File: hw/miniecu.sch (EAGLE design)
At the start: 60 parts

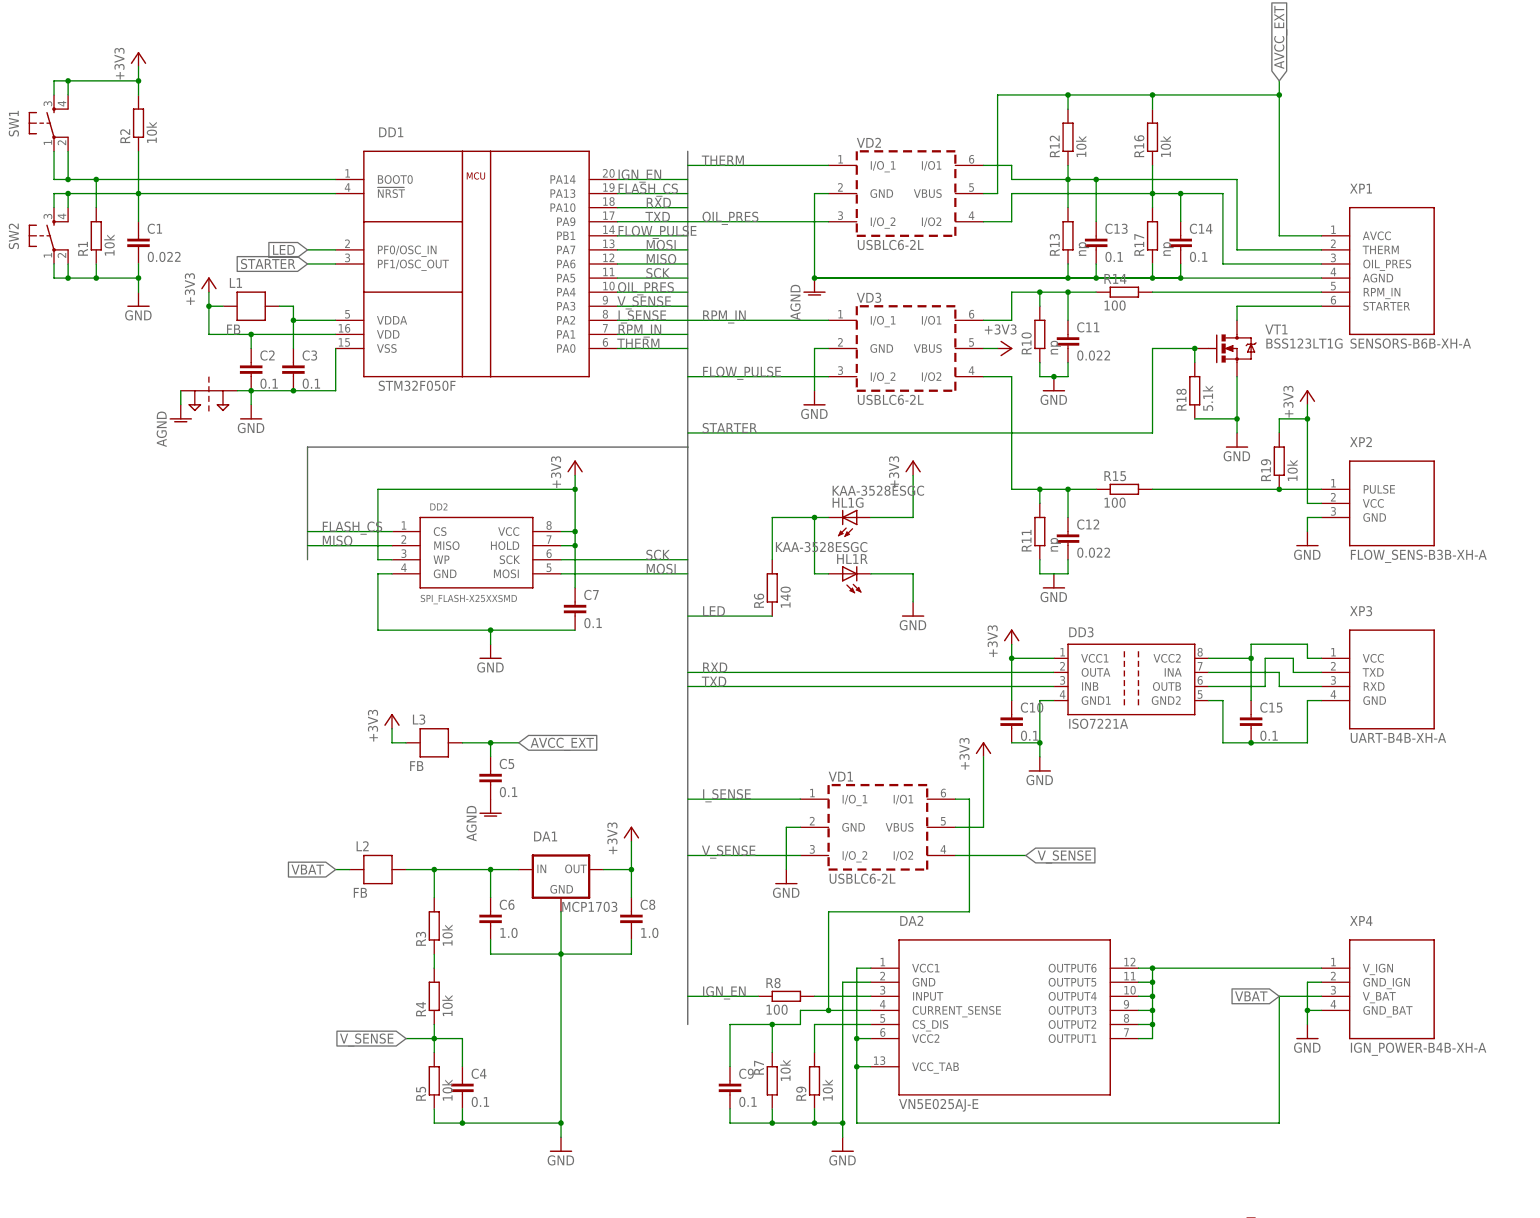
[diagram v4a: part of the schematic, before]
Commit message: sch: minimize BOM (by resistor values)
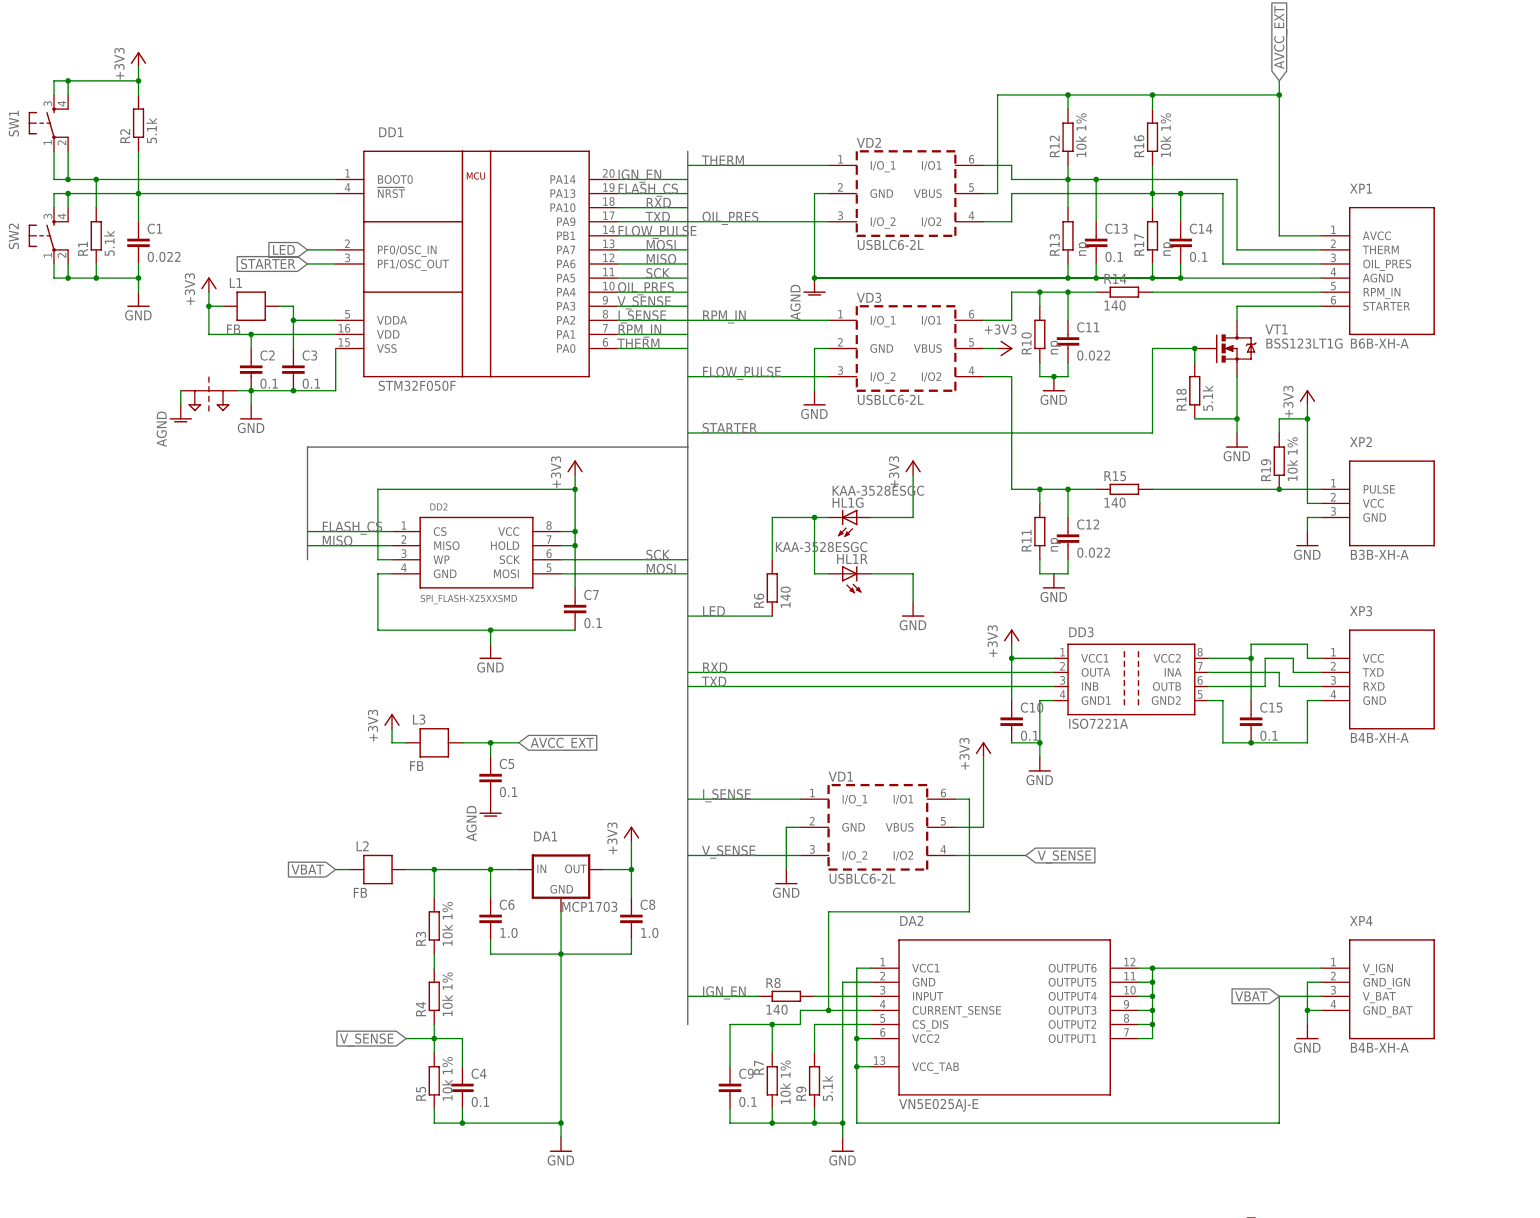
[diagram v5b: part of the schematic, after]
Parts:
- C1: device resistor:C-EUC0805 -> resistor:C-EUC0603
- R1, R2, R9: value 10k -> 5.1k
- R12, R16, R19, R3, R4, R5, R7: value 10k -> 10k 1%
- R14, R15, R8: value 100 -> 140
- XP1: value SENSORS-B6B-XH-A -> B6B-XH-A
- XP2: value FLOW_SENS-B3B-XH-A -> B3B-XH-A
- XP3: value UART-B4B-XH-A -> B4B-XH-A
- XP4: value IGN_POWER-B4B-XH-A -> B4B-XH-A
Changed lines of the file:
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@@
 <part name="DD2" library="SparkFun-DigitalIC" deviceset="SPI_FLASH-X25XX" device="SMD"/>
 <part name="DD3" library="texas" deviceset="ISO7221" device="" technology="A"/>
-<part name="XP2" library="miniecu-con" deviceset="FLOW_SENS" device="-B3B-XH-A"/>
-<part name="XP4" library="miniecu-con" deviceset="IGN_POWER" device="-B4B-XH-A"/>
-<part name="XP1" library="miniecu-con" deviceset="SENSORS" device="-B6B-XH-A"/>
-<part name="XP3" library="miniecu-con" deviceset="UART" device="-B4B-XH-A"/>
+<part name="XP2" library="miniecu-con" deviceset="FLOW_SENS" device="-B3B-XH-A" value="B3B-XH-A"/>
+<part name="XP4" library="miniecu-con" deviceset="IGN_POWER" device="-B4B-XH-A" value="B4B-XH-A"/>
+<part name="XP1" library="miniecu-con" deviceset="SENSORS" device="-B6B-XH-A" value="B6B-XH-A"/>
+<part name="XP3" library="miniecu-con" deviceset="UART" device="-B4B-XH-A" value="B4B-XH-A"/>
 <part name="C15" library="resistor" deviceset="C-EU" device="C0603" value="0.1"/>
 <part name="C10" library="resistor" deviceset="C-EU" device="C0603" value="0.1"/>
@@
 <part name="GND6" library="supply1" deviceset="GND" device=""/>
 <part name="R18" library="resistor" deviceset="R-EU_" device="R0603" value="5.1k"/>
-<part name="R14" library="resistor" deviceset="R-EU_" device="R0603" value="100"/>
+<part name="R14" library="resistor" deviceset="R-EU_" device="R0603" value="140"/>
 <part name="R10" library="resistor" deviceset="R-EU_" device="R0603" value="np"/>
 <part name="C11" library="resistor" deviceset="C-EU" device="C0603" value="0.022"/>
-<part name="R16" library="resistor" deviceset="R-EU_" device="R0805" value="10k"/>
-<part name="R12" library="resistor" deviceset="R-EU_" device="R0805" value="10k"/>
+<part name="R16" library="resistor" deviceset="R-EU_" device="R0805" value="10k 1%"/>
+<part name="R12" library="resistor" deviceset="R-EU_" device="R0805" value="10k 1%"/>
 <part name="R13" library="resistor" deviceset="R-EU_" device="R0805" value="np"/>
 <part name="R17" library="resistor" deviceset="R-EU_" device="R0805" value="np"/>
@@
 <part name="C13" library="resistor" deviceset="C-EU" device="C0603" value="0.1"/>
 <part name="GND7" library="supply1" deviceset="GND" device=""/>
-<part name="R15" library="resistor" deviceset="R-EU_" device="R0603" value="100"/>
+<part name="R15" library="resistor" deviceset="R-EU_" device="R0603" value="140"/>
 <part name="R11" library="resistor" deviceset="R-EU_" device="R0603" value="np"/>
 <part name="C12" library="resistor" deviceset="C-EU" device="C0603" value="0.022"/>
@@
 <part name="C5" library="resistor" deviceset="C-EU" device="C0603" value="0.1"/>
 <part name="+3V7" library="supply1" deviceset="+3V3" device=""/>
-<part name="C1" library="resistor" deviceset="C-EU" device="C0805" value="0.022"/>
+<part name="C1" library="resistor" deviceset="C-EU" device="C0603" value="0.022"/>
 <part name="GND10" library="supply1" deviceset="GND" device=""/>
 <part name="SW1" library="SparkFun-Electromechanical" deviceset="TAC_SWITCH" device="SMD"/>
@@
 <part name="C8" library="resistor" deviceset="C-EU" device="C0805" value="1.0"/>
 <part name="+3V9" library="supply1" deviceset="+3V3" device=""/>
-<part name="R4" library="resistor" deviceset="R-EU_" device="R0805" value="10k"/>
-<part name="R5" library="resistor" deviceset="R-EU_" device="R0805" value="10k"/>
+<part name="R4" library="resistor" deviceset="R-EU_" device="R0805" value="10k 1%"/>
+<part name="R5" library="resistor" deviceset="R-EU_" device="R0805" value="10k 1%"/>
 <part name="C4" library="resistor" deviceset="C-EU" device="C0603" value="0.1"/>
 <part name="VD1" library="usblc6" deviceset="USBLC6-2" device="SC6" value="USBLC6-2L"/>
 <part name="GND12" library="supply1" deviceset="GND" device=""/>
 <part name="DA2" library="power-ic" deviceset="VN5E025AJ" device="-E"/>
-<part name="R8" library="resistor" deviceset="R-EU_" device="R0603" value="100"/>
+<part name="R8" library="resistor" deviceset="R-EU_" device="R0603" value="140"/>
 <part name="GND13" library="supply1" deviceset="GND" device=""/>
-<part name="R9" library="resistor" deviceset="R-EU_" device="R0603" value="10k"/>
-<part name="R7" library="resistor" deviceset="R-EU_" device="R0805" value="10k"/>
+<part name="R9" library="resistor" deviceset="R-EU_" device="R0603" value="5.1k"/>
+<part name="R7" library="resistor" deviceset="R-EU_" device="R0805" value="10k 1%"/>
 <part name="C9" library="resistor" deviceset="C-EU" device="C0603" value="0.1"/>
 <part name="FRAME1" library="SparkFun-Aesthetics" deviceset="FRAME-A3" device=""/>
-<part name="R19" library="resistor" deviceset="R-EU_" device="R0805" value="10k"/>
+<part name="R19" library="resistor" deviceset="R-EU_" device="R0805" value="10k 1%"/>
 <part name="HL1" library="led2" deviceset="KAA-3528ESGC" device=""/>
 <part name="GND14" library="supply1" deviceset="GND" device=""/>
@@
 <part name="H3" library="holes" deviceset="MOUNT-HOLE" device="3.2"/>
 <part name="H4" library="holes" deviceset="MOUNT-HOLE" device="3.2"/>
-<part name="R1" library="resistor" deviceset="R-EU_" device="R0603" value="10k"/>
-<part name="R2" library="resistor" deviceset="R-EU_" device="R0603" value="10k"/>
+<part name="R1" library="resistor" deviceset="R-EU_" device="R0603" value="5.1k"/>
+<part name="R2" library="resistor" deviceset="R-EU_" device="R0603" value="5.1k"/>
 <part name="+3V10" library="supply1" deviceset="+3V3" device=""/>
-<part name="R3" library="resistor" deviceset="R-EU_" device="R0805" value="10k"/>
+<part name="R3" library="resistor" deviceset="R-EU_" device="R0805" value="10k 1%"/>
 <part name="LOGO1" library="SparkFun-Aesthetics" deviceset="OSHW-LOGO" device="L"/>
 <part name="U$1" library="miniecu" deviceset="MINIECU_LOGO" device=""/>

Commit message: hw: release hw v1b, update gerbers
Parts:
- renumbered U$1 to LOGO2
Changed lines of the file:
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@@
 <part name="R3" library="resistor" deviceset="R-EU_" device="R0805" value="10k 1%"/>
 <part name="LOGO1" library="SparkFun-Aesthetics" deviceset="OSHW-LOGO" device="L"/>
-<part name="U$1" library="miniecu" deviceset="MINIECU_LOGO" device=""/>
+<part name="LOGO2" library="miniecu" deviceset="MINIECU_LOGO" device=""/>
 </parts>
 <sheets>
@@
 <instance part="R3" gate="G$1" x="-10.16" y="-111.76" rot="R90"/>
 <instance part="LOGO1" gate="G$1" x="137.16" y="-170.18"/>
-<instance part="U$1" gate="G$1" x="109.22" y="-175.26"/>
+<instance part="LOGO2" gate="G$1" x="109.22" y="-175.26"/>
 </instances>
 <busses>
